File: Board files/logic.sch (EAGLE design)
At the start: 19 parts, among them U2 LD1117, U3 LM2662

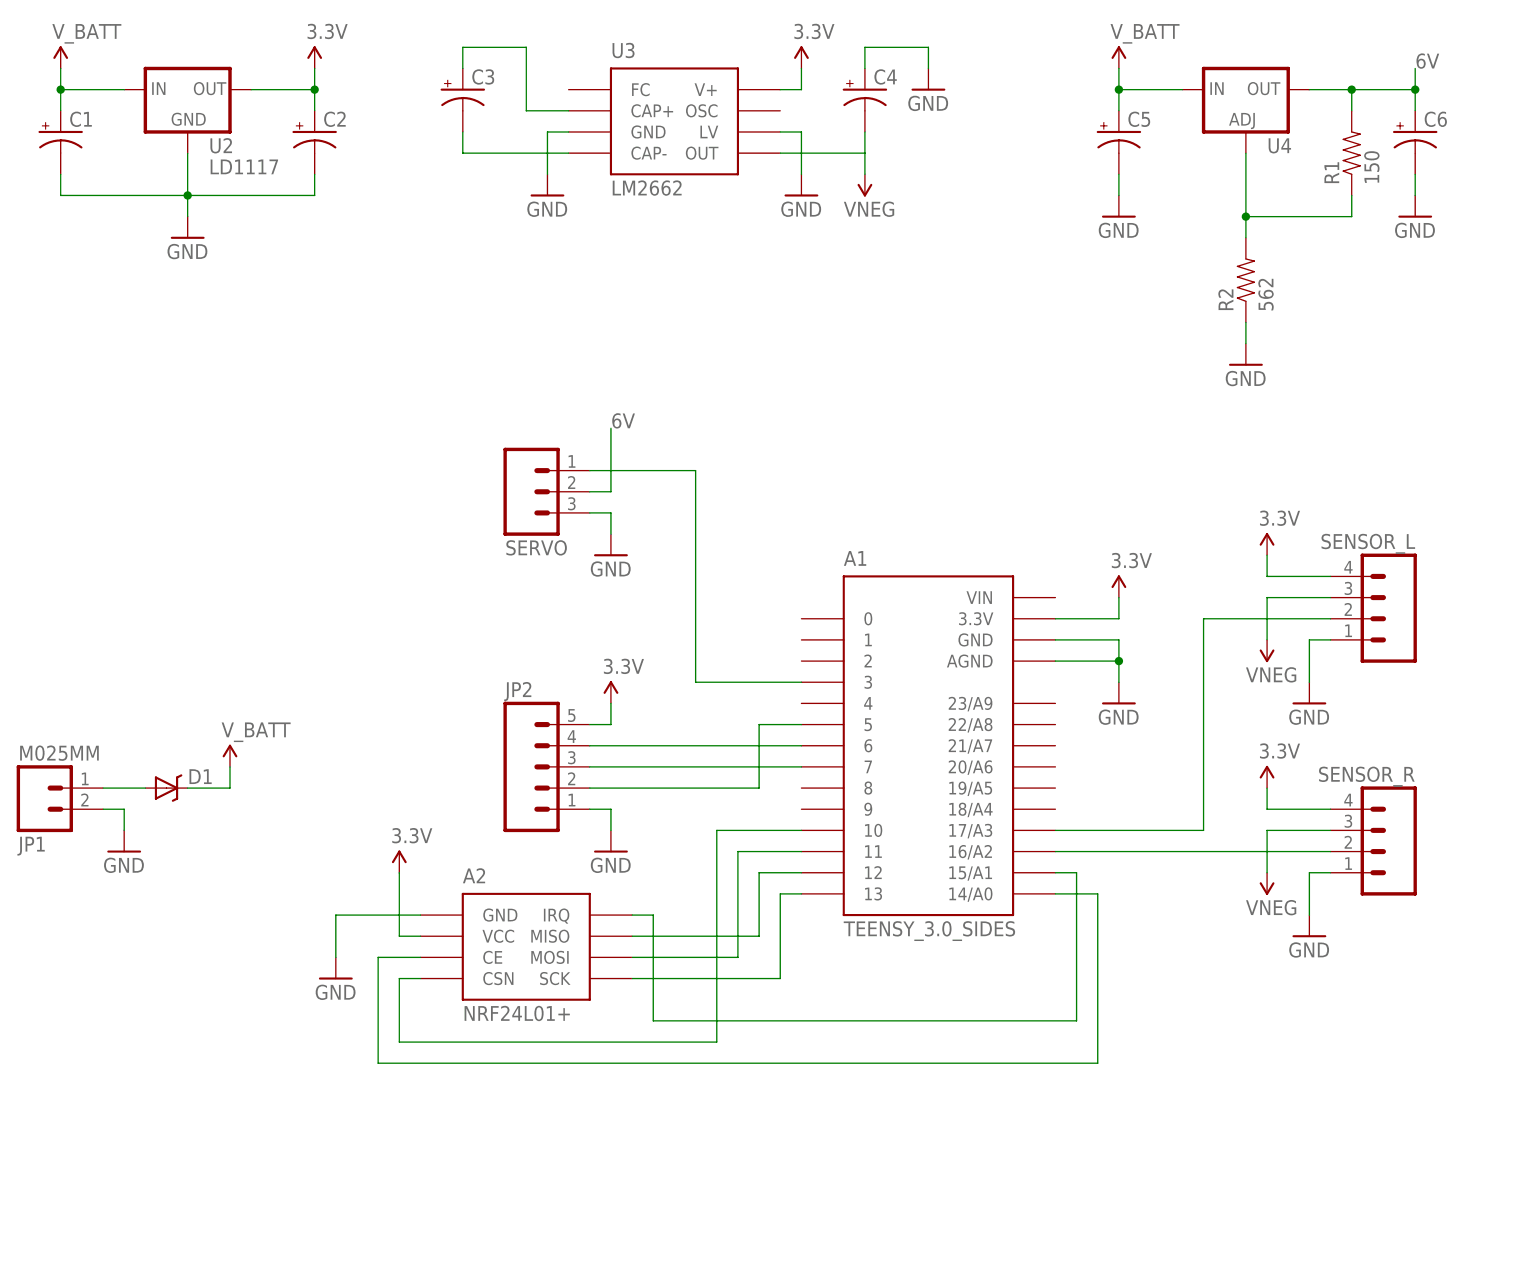
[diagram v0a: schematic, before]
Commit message: Finished logic board layout
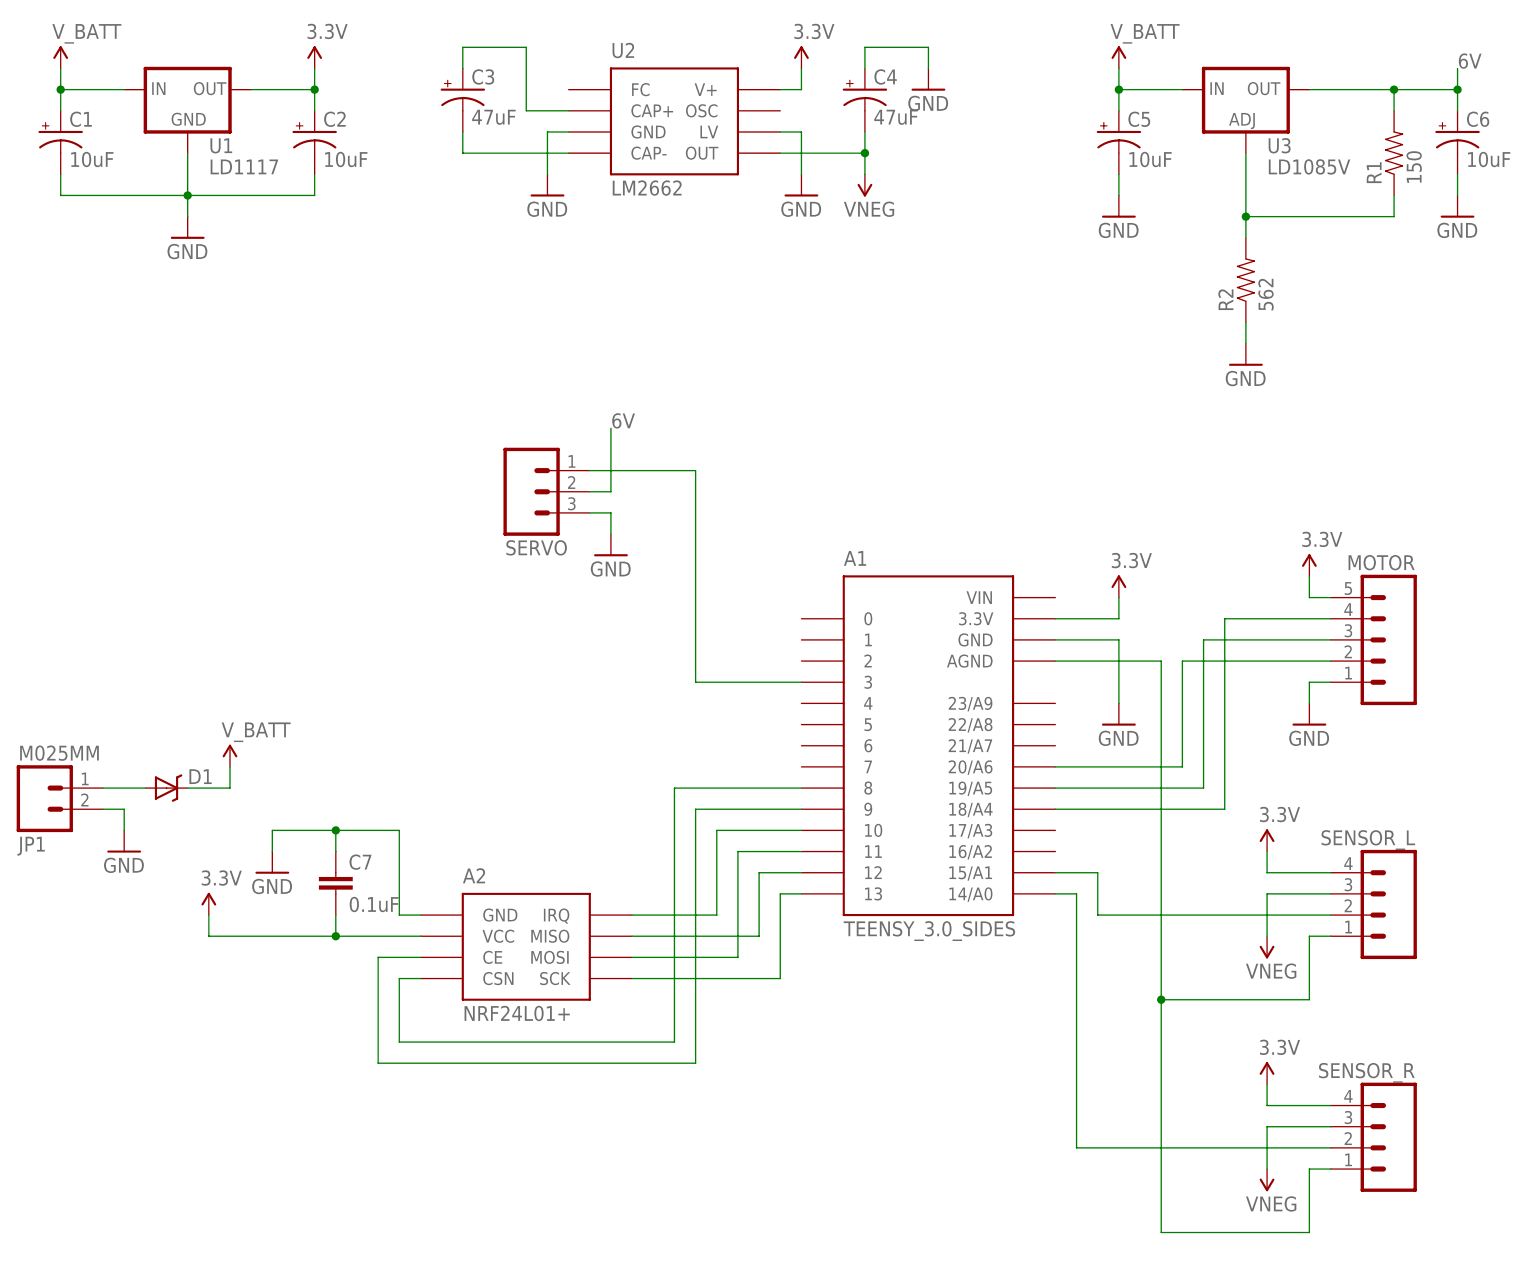
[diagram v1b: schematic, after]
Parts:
- removed JP2: (no value), SparkFun-Connectors:M05LOCK
- removed U4: (no value), v-reg:LM317TS
- added C7: 0.1uF, SparkFun-Capacitors:CAP0805
- added MOTOR: (no value), SparkFun-Connectors:M05LOCK
- added U1: LD1117, Custom:LD1117
- C1, C2, C5, C6: value (none) -> 10uF
- C3, C4: value (none) -> 47uF
- U2: value LD1117 -> LM2662; device Custom:LD1117 -> Custom:LM2662
- U3: value LM2662 -> LD1085V; device Custom:LM2662 -> v-reg:LM317TS
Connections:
- new net N$17: A1.18/A4, MOTOR.4
- net 3.3V: now also C7.2, MOTOR.5, U1.OUT, U2.V+; no longer JP2.5, U2.OUT, U3.V+
- net 6V: now also U3.OUT; no longer U4.OUT
- net GND: now also C7.1, MOTOR.1, U1.GND, U2.LV; no longer A1.AGND, JP2.1, SENSOR_L.1, SENSOR_R.1, U3.GND, U3.LV
- net N$10: now also A1.9; no longer A1.14/A0
- net N$12: now also A1.AGND, SENSOR_L.1, SENSOR_R.1; no longer A1.16/A2, SENSOR_R.2
- net N$13: now also A1.15/A1; no longer A1.17/A3
- net N$14: now also A1.14/A0, SENSOR_R.2; no longer A1.5, JP2.2
- net N$15: now also A1.20/A6, MOTOR.2; no longer A1.6, JP2.4
- net N$16: now also A1.19/A5, MOTOR.3; no longer A1.7, JP2.3
- net N$2: now also U2.CAP+; no longer U3.CAP+
- net N$3: now also U2.CAP-; no longer U3.CAP-
- net N$4: now also U3.ADJ; no longer U4.ADJ
- net N$8: now also A1.8; no longer A1.10
- net N$9: now also A1.10; no longer A1.15/A1
- net VNEG: now also U2.OUT; no longer U3.OUT
- net V_BATT: now also U1.IN, U3.IN; no longer U2.IN, U4.IN
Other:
- moved on the sheet: C6, R1, SENSOR_L, SENSOR_R

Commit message: Changed logic board layout
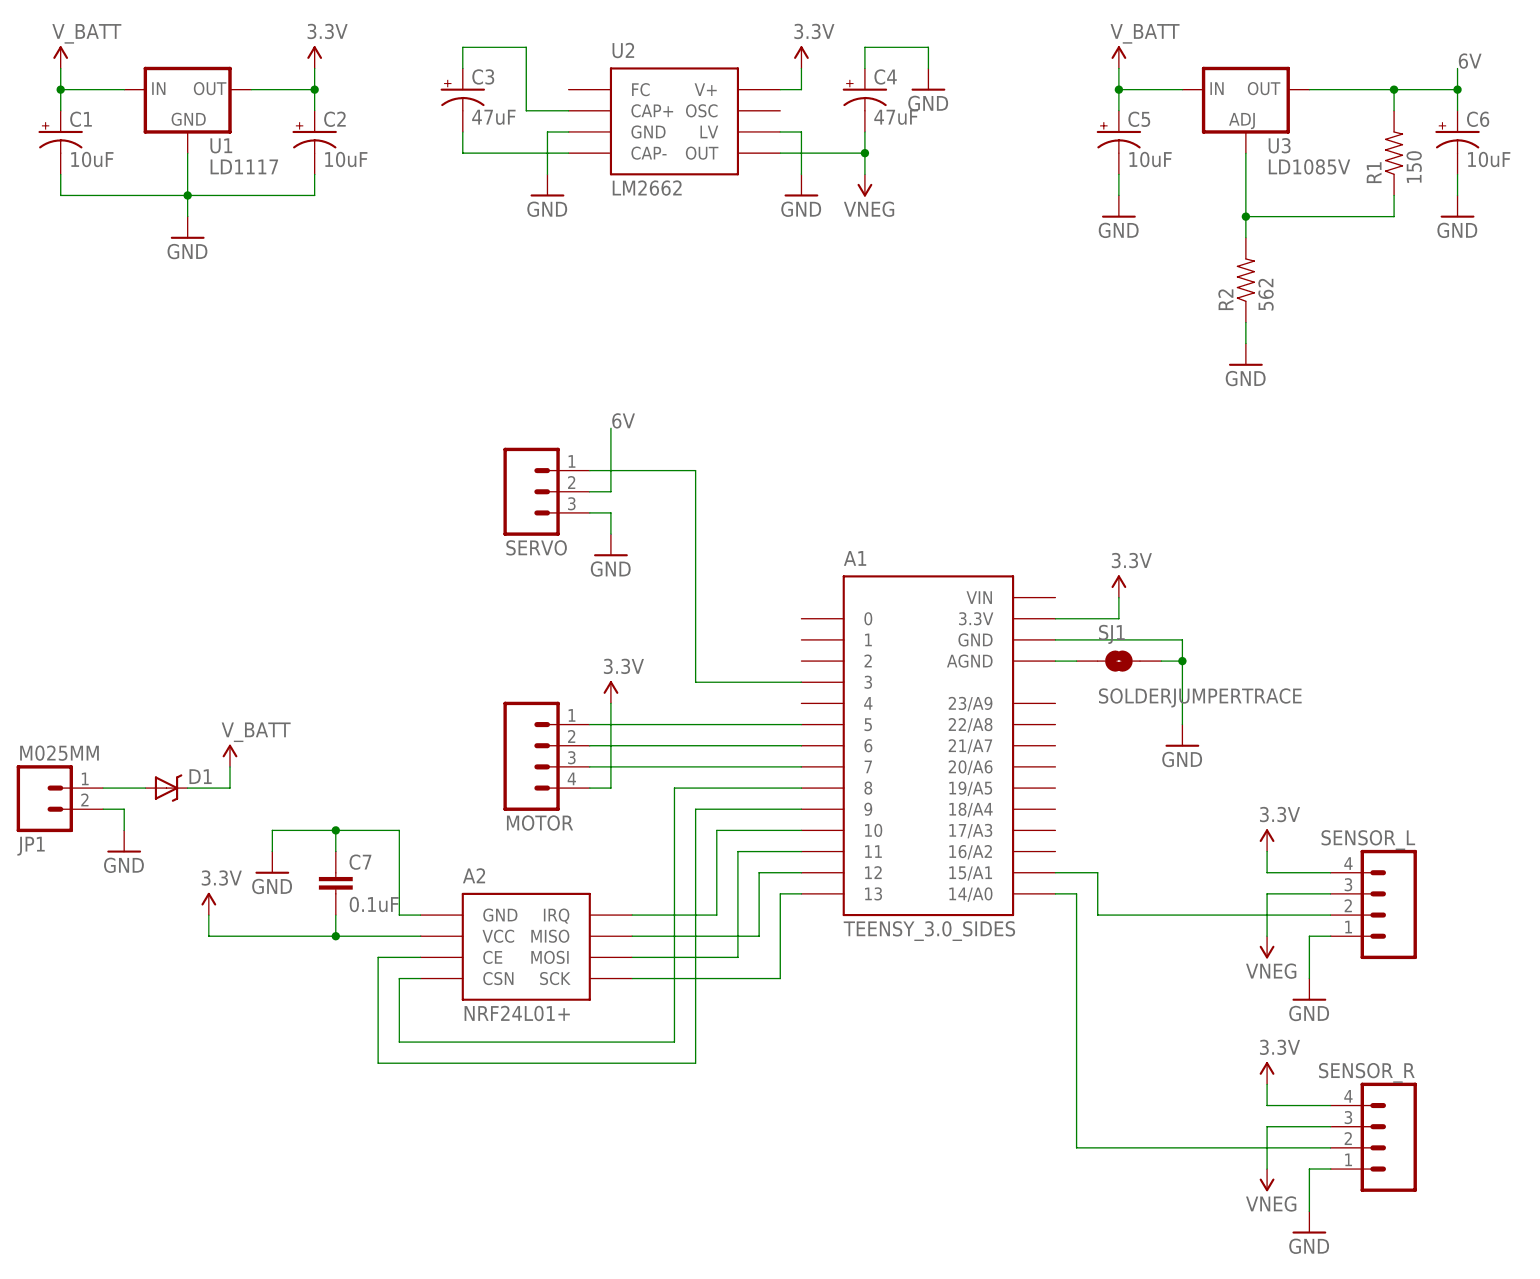
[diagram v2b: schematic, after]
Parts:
- added SJ1: SOLDERJUMPERTRACE, SparkFun-Passives:SOLDERJUMPERTRACE
- MOTOR: device SparkFun-Connectors:M05LOCK -> SparkFun-Connectors:M04LOCK
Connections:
- net 3.3V: now also MOTOR.4; no longer MOTOR.5
- net GND: now also SENSOR_L.1, SENSOR_R.1, SJ1.2; no longer MOTOR.1
- net N$12: now also SJ1.1; no longer SENSOR_L.1, SENSOR_R.1
- net N$15: now also A1.5, MOTOR.1; no longer A1.20/A6, MOTOR.2
- net N$16: now also A1.6, MOTOR.2; no longer A1.19/A5, MOTOR.3
- net N$17: now also A1.7, MOTOR.3; no longer A1.18/A4, MOTOR.4
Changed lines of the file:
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@@
 <part name="GND10" library="SparkFun-Aesthetics" deviceset="GND" device=""/>
 <part name="SUPPLY8" library="SparkFun-Aesthetics" deviceset="3.3V" device=""/>
-<part name="MOTOR" library="SparkFun-Connectors" deviceset="M05" device="LOCK"/>
 <part name="SUPPLY9" library="SparkFun-Aesthetics" deviceset="VNEG" device=""/>
 <part name="SUPPLY10" library="SparkFun-Aesthetics" deviceset="VNEG" device=""/>
@@
 <part name="SUPPLY12" library="SparkFun-Aesthetics" deviceset="3.3V" device=""/>
 <part name="GND13" library="SparkFun-Aesthetics" deviceset="GND" device=""/>
-<part name="GND14" library="SparkFun-Aesthetics" deviceset="GND" device=""/>
 <part name="SUPPLY13" library="SparkFun-Aesthetics" deviceset="3.3V" device=""/>
 <part name="C7" library="SparkFun-Capacitors" deviceset="CAP" device="0805" value="0.1uF"/>
+<part name="MOTOR" library="SparkFun-Connectors" deviceset="M04" device="LOCK"/>
+<part name="GND11" library="SparkFun-Aesthetics" deviceset="GND" device=""/>
+<part name="GND12" library="SparkFun-Aesthetics" deviceset="GND" device=""/>
+<part name="SJ1" library="SparkFun-Passives" deviceset="SOLDERJUMPER" device="TRACE"/>
 </parts>
 <sheets>
@@
 <instance part="GND8" gate="1" x="152.4" y="73.66"/>
 <instance part="SUPPLY7" gate="G$1" x="137.16" y="45.72"/>
-<instance part="GND9" gate="1" x="137.16" y="30.48"/>
+<instance part="GND9" gate="1" x="144.78" y="27.94"/>
 <instance part="C1" gate="G$1" x="10.16" y="101.6"/>
 <instance part="C2" gate="G$1" x="40.64" y="101.6"/>
@@
 <instance part="GND10" gate="1" x="35.56" y="12.7"/>
 <instance part="SUPPLY8" gate="G$1" x="27.94" y="7.62"/>
-<instance part="MOTOR" gate="G$1" x="170.18" y="40.64" rot="MR0"/>
 <instance part="SUPPLY9" gate="G$2" x="154.94" y="-25.4"/>
 <instance part="SUPPLY10" gate="G$2" x="154.94" y="2.54"/>
@@
 <instance part="SUPPLY12" gate="G$1" x="154.94" y="-12.7"/>
 <instance part="GND13" gate="1" x="76.2" y="50.8"/>
-<instance part="GND14" gate="1" x="160.02" y="30.48"/>
-<instance part="SUPPLY13" gate="G$1" x="160.02" y="48.26"/>
+<instance part="SUPPLY13" gate="G$1" x="76.2" y="33.02"/>
 <instance part="C7" gate="G$1" x="43.18" y="10.16"/>
+<instance part="MOTOR" gate="G$1" x="68.58" y="27.94" rot="MR180"/>
+<instance part="GND11" gate="1" x="160.02" y="-2.54"/>
+<instance part="GND12" gate="1" x="160.02" y="-30.48"/>
+<instance part="SJ1" gate="1" x="137.16" y="38.1"/>
 </instances>
 <busses>
@@
 <segment>
 <pinref part="GND9" gate="1" pin="GND"/>
-<wire x1="129.54" y1="40.64" x2="137.16" y2="40.64" width="0.1524" layer="91"/>
-<wire x1="137.16" y1="40.64" x2="137.16" y2="33.02" width="0.1524" layer="91"/>
+<wire x1="129.54" y1="40.64" x2="144.78" y2="40.64" width="0.1524" layer="91"/>
+<wire x1="144.78" y1="40.64" x2="144.78" y2="38.1" width="0.1524" layer="91"/>
 <pinref part="A1" gate="G$1" pin="GND"/>
+<pinref part="SJ1" gate="1" pin="2"/>
+<wire x1="144.78" y1="38.1" x2="144.78" y2="30.48" width="0.1524" layer="91"/>
+<wire x1="142.24" y1="38.1" x2="144.78" y2="38.1" width="0.1524" layer="91"/>
+<junction x="144.78" y="38.1"/>
 </segment>
 <segment>
@@
 <wire x1="73.66" y1="55.88" x2="76.2" y2="55.88" width="0.1524" layer="91"/>
 <wire x1="76.2" y1="55.88" x2="76.2" y2="53.34" width="0.1524" layer="91"/>
-</segment>
-<segment>
-<pinref part="MOTOR" gate="G$1" pin="1"/>
-<pinref part="GND14" gate="1" pin="GND"/>
-<wire x1="162.56" y1="35.56" x2="160.02" y2="35.56" width="0.1524" layer="91"/>
-<wire x1="160.02" y1="35.56" x2="160.02" y2="33.02" width="0.1524" layer="91"/>
 </segment>
 <segment>
@@
 <junction x="43.18" y="17.78"/>
 </segment>
+<segment>
+<pinref part="SENSOR_L" gate="G$1" pin="1"/>
+<wire x1="160.02" y1="5.08" x2="162.56" y2="5.08" width="0.1524" layer="91"/>
+<wire x1="160.02" y1="0" x2="160.02" y2="5.08" width="0.1524" layer="91"/>
+<pinref part="GND11" gate="1" pin="GND"/>
+</segment>
+<segment>
+<pinref part="SENSOR_R" gate="G$1" pin="1"/>
+<wire x1="160.02" y1="-22.86" x2="162.56" y2="-22.86" width="0.1524" layer="91"/>
+<wire x1="160.02" y1="-27.94" x2="160.02" y2="-22.86" width="0.1524" layer="91"/>
+<pinref part="GND12" gate="1" pin="GND"/>
+</segment>
 </net>
 <net name="V_BATT" class="0">
@@
 </segment>
 <segment>
-<pinref part="MOTOR" gate="G$1" pin="5"/>
 <pinref part="SUPPLY13" gate="G$1" pin="3.3V"/>
-<wire x1="162.56" y1="45.72" x2="160.02" y2="45.72" width="0.1524" layer="91"/>
-<wire x1="160.02" y1="45.72" x2="160.02" y2="48.26" width="0.1524" layer="91"/>
+<wire x1="73.66" y1="22.86" x2="76.2" y2="22.86" width="0.1524" layer="91"/>
+<wire x1="76.2" y1="22.86" x2="76.2" y2="33.02" width="0.1524" layer="91"/>
+<pinref part="MOTOR" gate="G$1" pin="4"/>
 </segment>
 <segment>
@@
 <segment>
 <pinref part="A1" gate="G$1" pin="AGND"/>
-<wire x1="129.54" y1="38.1" x2="142.24" y2="38.1" width="0.1524" layer="91"/>
-<wire x1="142.24" y1="38.1" x2="142.24" y2="-2.54" width="0.1524" layer="91"/>
-<wire x1="142.24" y1="-2.54" x2="160.02" y2="-2.54" width="0.1524" layer="91"/>
-<wire x1="160.02" y1="-2.54" x2="160.02" y2="5.08" width="0.1524" layer="91"/>
-<pinref part="SENSOR_L" gate="G$1" pin="1"/>
-<wire x1="160.02" y1="5.08" x2="162.56" y2="5.08" width="0.1524" layer="91"/>
-<wire x1="142.24" y1="-2.54" x2="142.24" y2="-30.48" width="0.1524" layer="91"/>
-<wire x1="142.24" y1="-30.48" x2="160.02" y2="-30.48" width="0.1524" layer="91"/>
-<wire x1="160.02" y1="-30.48" x2="160.02" y2="-22.86" width="0.1524" layer="91"/>
-<pinref part="SENSOR_R" gate="G$1" pin="1"/>
-<wire x1="160.02" y1="-22.86" x2="162.56" y2="-22.86" width="0.1524" layer="91"/>
-<junction x="142.24" y="-2.54"/>
+<wire x1="129.54" y1="38.1" x2="132.08" y2="38.1" width="0.1524" layer="91"/>
+<pinref part="SJ1" gate="1" pin="1"/>
 </segment>
 </net>
@@
 <net name="N$15" class="0">
 <segment>
+<pinref part="MOTOR" gate="G$1" pin="1"/>
+<pinref part="A1" gate="G$1" pin="5"/>
+<wire x1="73.66" y1="30.48" x2="99.06" y2="30.48" width="0.1524" layer="91"/>
+</segment>
+</net>
+<net name="N$16" class="0">
+<segment>
 <pinref part="MOTOR" gate="G$1" pin="2"/>
-<wire x1="162.56" y1="38.1" x2="144.78" y2="38.1" width="0.1524" layer="91"/>
-<wire x1="144.78" y1="38.1" x2="144.78" y2="25.4" width="0.1524" layer="91"/>
-<pinref part="A1" gate="G$1" pin="20/A6"/>
-<wire x1="144.78" y1="25.4" x2="129.54" y2="25.4" width="0.1524" layer="91"/>
-</segment>
-</net>
-<net name="N$16" class="0">
+<pinref part="A1" gate="G$1" pin="6"/>
+<wire x1="73.66" y1="27.94" x2="99.06" y2="27.94" width="0.1524" layer="91"/>
+</segment>
+</net>
+<net name="N$17" class="0">
 <segment>
 <pinref part="MOTOR" gate="G$1" pin="3"/>
-<wire x1="162.56" y1="40.64" x2="147.32" y2="40.64" width="0.1524" layer="91"/>
-<wire x1="147.32" y1="40.64" x2="147.32" y2="22.86" width="0.1524" layer="91"/>
-<pinref part="A1" gate="G$1" pin="19/A5"/>
-<wire x1="147.32" y1="22.86" x2="129.54" y2="22.86" width="0.1524" layer="91"/>
-</segment>
-</net>
-<net name="N$17" class="0">
-<segment>
-<pinref part="MOTOR" gate="G$1" pin="4"/>
-<wire x1="162.56" y1="43.18" x2="149.86" y2="43.18" width="0.1524" layer="91"/>
-<wire x1="149.86" y1="43.18" x2="149.86" y2="20.32" width="0.1524" layer="91"/>
-<pinref part="A1" gate="G$1" pin="18/A4"/>
-<wire x1="149.86" y1="20.32" x2="129.54" y2="20.32" width="0.1524" layer="91"/>
-</segment>
-</net>
+<pinref part="A1" gate="G$1" pin="7"/>
+<wire x1="73.66" y1="25.4" x2="99.06" y2="25.4" width="0.1524" layer="91"/>
+</segment>
+</net>
